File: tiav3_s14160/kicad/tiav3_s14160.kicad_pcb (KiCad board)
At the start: 4 copper layers, 25.3 x 25.3 mm, 22 parts, among them J1 SSQ-103-01-G-D, J2 Conn_Coaxial, U1 OPA847IDBVT

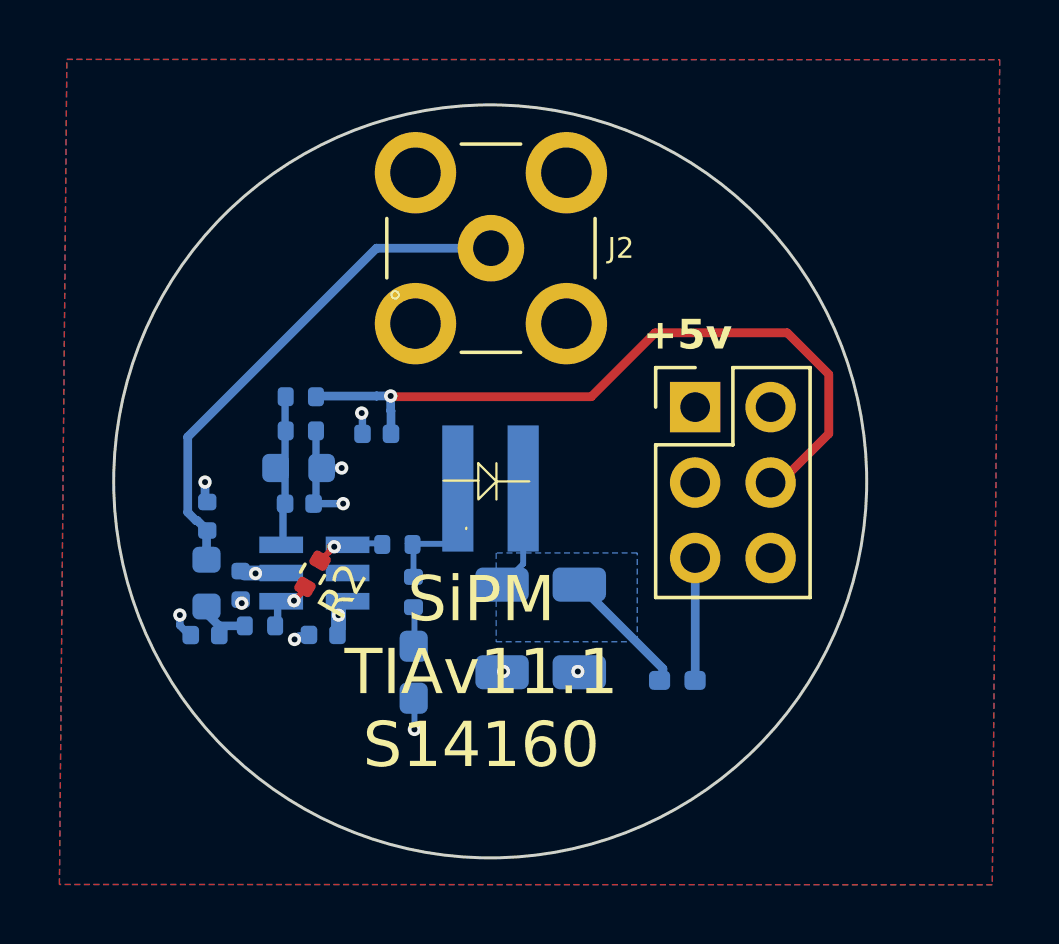
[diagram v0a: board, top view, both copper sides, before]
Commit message: Tune tiav3 LPF values and export gerbers
Update LPF component values (560nH->330nH, 120pF->62pF) and tighten via diameter/drill DRC. Redirect plot/step outputs to ../manufacturing/ and commit the generated gerber set.
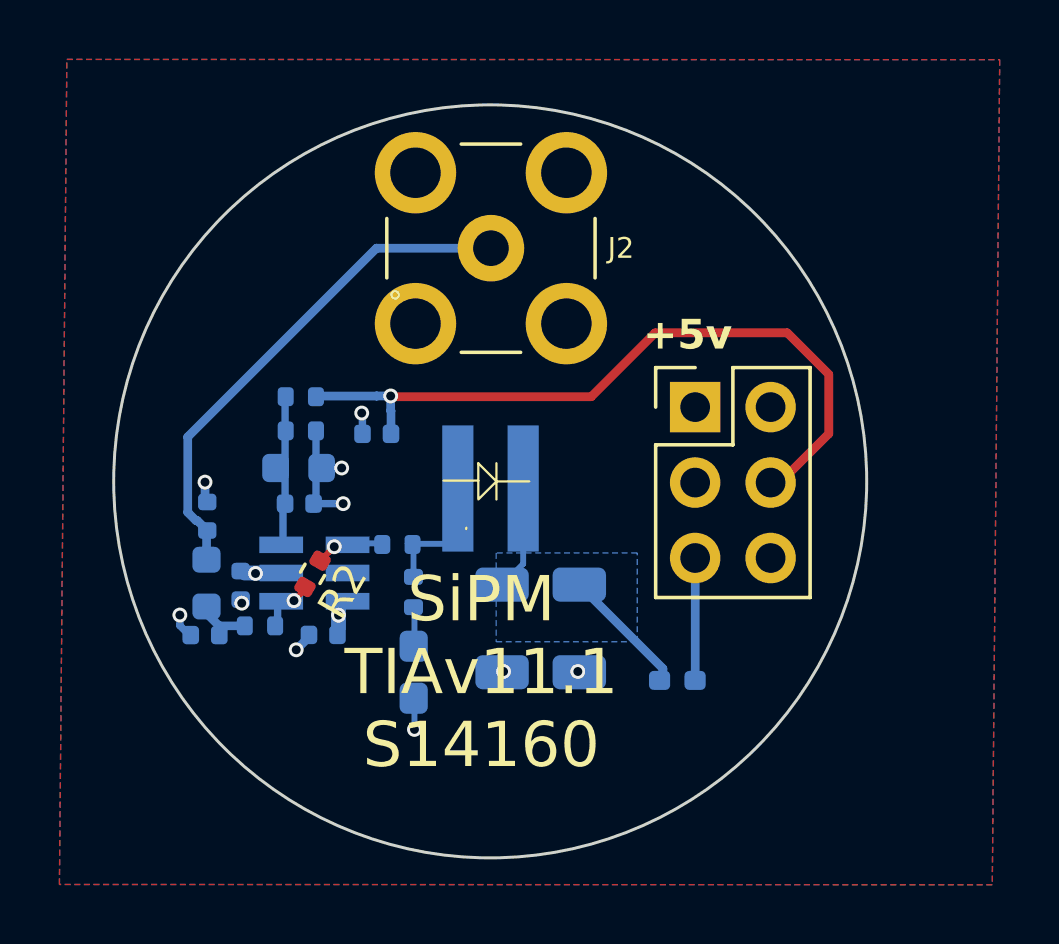
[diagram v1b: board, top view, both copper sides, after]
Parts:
- C2: value 120pF -> 62pF
- C3: value 120p -> 62pF
- L2: value 560nH -> 330nH
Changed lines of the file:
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@@
 			)
 		)
-		(property "Datasheet" ""
+		(property "Datasheet" "~"
 			(at 0 0 240)
 			(layer "F.Fab")
@@
 			)
 		)
-		(property "Datasheet" " ~"
+		(property "Datasheet" "~"
 			(at 0 0 0)
 			(layer "F.Fab")
@@
 			)
 		)
-		(property "Datasheet" ""
+		(property "Datasheet" "~"
 			(at 0 0 180)
 			(layer "B.Fab")
@@
 			)
 		)
+		(property "Voltage" "10V"
+			(at 0 0 0)
+			(unlocked yes)
+			(layer "B.Fab")
+			(hide yes)
+			(effects
+				(font
+					(size 1 1)
+					(thickness 0.15)
+				)
+				(justify mirror)
+			)
+		)
 		(property ki_fp_filters "C_*")
 		(sheetname "/")
@@
 			)
 		)
-		(property "Datasheet" ""
+		(property "Datasheet" "~"
 			(at 0 0 0)
 			(layer "B.Fab")
@@
 			)
 		)
-		(property "Datasheet" ""
+		(property "Datasheet" "~"
 			(at 0 0 0)
 			(layer "B.Fab")
@@
 			)
 		)
-		(property "Datasheet" ""
+		(property "Datasheet" "~"
 			(at 0 0 270)
 			(layer "B.Fab")
@@
 			)
 		)
-		(property "Datasheet" ""
+		(property "Datasheet" "~"
 			(at 0 0 0)
 			(layer "B.Fab")
@@
 			)
 		)
-		(property "Value" "120p"
+		(property "Value" "62pF"
 			(at 0 -1.16 90)
 			(layer "B.Fab")
@@
 			)
 		)
-		(property "Value" "120pF"
+		(property "Value" "62pF"
 			(at 0 -1.16 0)
 			(layer "B.Fab")
@@
 			)
 		)
-		(property "Value" "560nH"
+		(property "Value" "330nH"
 			(at 0 -1.43 270)
 			(layer "B.Fab")
@@
 			)
 		)
+		(property "part" "MLF1005GR56JTD25"
+			(at 0 0 90)
+			(unlocked yes)
+			(layer "B.Fab")
+			(hide yes)
+			(effects
+				(font
+					(size 1 1)
+					(thickness 0.15)
+				)
+				(justify mirror)
+			)
+		)
 		(property ki_fp_filters "Choke_* *Coil* Inductor_* L_*")
 		(sheetname "/")
@@
 	(via
 		(at 191.636 104.1)
-		(size 0.45)
-		(drill 0.2)
+		(size 0.5)
+		(drill 0.3)
 		(layers "F.Cu" "B.Cu")
 		(net 1)
@@
 	(via
 		(at 189.552584 104.499582)
-		(size 0.45)
-		(drill 0.2)
+		(size 0.5)
+		(drill 0.3)
 		(layers "F.Cu" "B.Cu")
 		(net 1)
@@
 	(via
 		(at 200.45 106.4)
-		(size 0.45)
-		(drill 0.2)
+		(size 0.5)
+		(drill 0.3)
 		(layers "F.Cu" "B.Cu")
 		(net 1)
@@
 	(via
 		(at 202.95 106.4)
-		(size 0.45)
-		(drill 0.2)
+		(size 0.5)
+		(drill 0.3)
 		(layers "F.Cu" "B.Cu")
 		(net 1)
@@
 	(via
 		(at 195.675 97.7)
-		(size 0.45)
-		(drill 0.2)
+		(size 0.5)
+		(drill 0.3)
 		(layers "F.Cu" "B.Cu")
 		(net 1)
@@
 	(via
 		(at 197.45 108.35)
-		(size 0.45)
-		(drill 0.2)
+		(size 0.5)
+		(drill 0.3)
 		(layers "F.Cu" "B.Cu")
 		(net 1)
@@
 	(via
 		(at 190.4 100.025)
-		(size 0.45)
-		(drill 0.2)
+		(size 0.5)
+		(drill 0.3)
 		(layers "F.Cu" "B.Cu")
 		(net 1)
@@
 	(via
 		(at 195.05 100.75)
-		(size 0.45)
-		(drill 0.2)
+		(size 0.5)
+		(drill 0.3)
 		(layers "F.Cu" "B.Cu")
 		(net 1)
 	)
 	(via
-		(at 193.414 105.3208)
-		(size 0.45)
-		(drill 0.2)
+		(at 193.47 105.67)
+		(size 0.5)
+		(drill 0.3)
 		(layers "F.Cu" "B.Cu")
 		(net 1)
@@
 	(via
 		(at 195 99.55)
-		(size 0.45)
-		(drill 0.2)
+		(size 0.5)
+		(drill 0.3)
 		(layers "F.Cu" "B.Cu")
 		(net 1)
@@
 	)
 	(segment
+		(start 193.9128 105.2272)
+		(end 193.9128 105.2192)
+		(width 0.29337)
+		(layer "B.Cu")
+		(net 1)
+	)
+	(segment
 		(start 194.055 100.75)
 		(end 194.135 100.67)
@@
 	)
 	(segment
-		(start 190.4 100.55)
-		(end 190.4 100.025)
+		(start 193.9128 105.2192)
+		(end 193.982 105.15)
 		(width 0.29337)
 		(layer "B.Cu")
@@
 	)
 	(segment
-		(start 195.675 97.7)
-		(end 195.65 97.725)
-		(width 0.25)
-		(layer "B.Cu")
-		(net 1)
-	)
-	(segment
-		(start 193.9128 105.2192)
-		(end 193.982 105.15)
+		(start 190.4 100.55)
+		(end 190.4 100.025)
 		(width 0.29337)
 		(layer "B.Cu")
@@
 	)
 	(segment
-		(start 193.5664 105.2192)
-		(end 193.9128 105.2192)
-		(width 0.29337)
+		(start 195.675 97.7)
+		(end 195.65 97.725)
+		(width 0.25)
 		(layer "B.Cu")
 		(net 1)
@@
 	)
 	(segment
+		(start 193.47 105.67)
+		(end 193.9128 105.2272)
+		(width 0.29337)
+		(layer "B.Cu")
+		(net 1)
+	)
+	(segment
 		(start 195.7 97.725)
 		(end 195.675 97.7)
@@
 	(via
 		(at 194.894 104.504)
-		(size 0.45)
-		(drill 0.2)
+		(size 0.5)
+		(drill 0.3)
 		(layers "F.Cu" "B.Cu")
 		(net 4)
@@
 	(via
 		(at 192.1 103.1)
-		(size 0.45)
-		(drill 0.2)
+		(size 0.5)
+		(drill 0.3)
 		(layers "F.Cu" "B.Cu")
 		(net 5)
@@
 	(via
 		(at 193.394 104.014599)
-		(size 0.45)
-		(drill 0.2)
+		(size 0.5)
+		(drill 0.3)
 		(layers "F.Cu" "B.Cu")
 		(net 6)
@@
 	(via
 		(at 196.65 97.125)
-		(size 0.45)
-		(drill 0.2)
+		(size 0.5)
+		(drill 0.3)
 		(layers "F.Cu" "B.Cu")
 		(net 11)
@@
 	(via
 		(at 194.75 102.2)
-		(size 0.45)
-		(drill 0.2)
+		(size 0.5)
+		(drill 0.3)
 		(layers "F.Cu" "B.Cu")
 		(net 13)
